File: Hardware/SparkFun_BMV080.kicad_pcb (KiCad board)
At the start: 2 copper layers, 25.4 x 14 mm, 37 parts, among them J1 Qwiic_RA, J2 Qwiic_RA, J3 Conn_01x06, J4 Conn_01x01, U1 BMV080

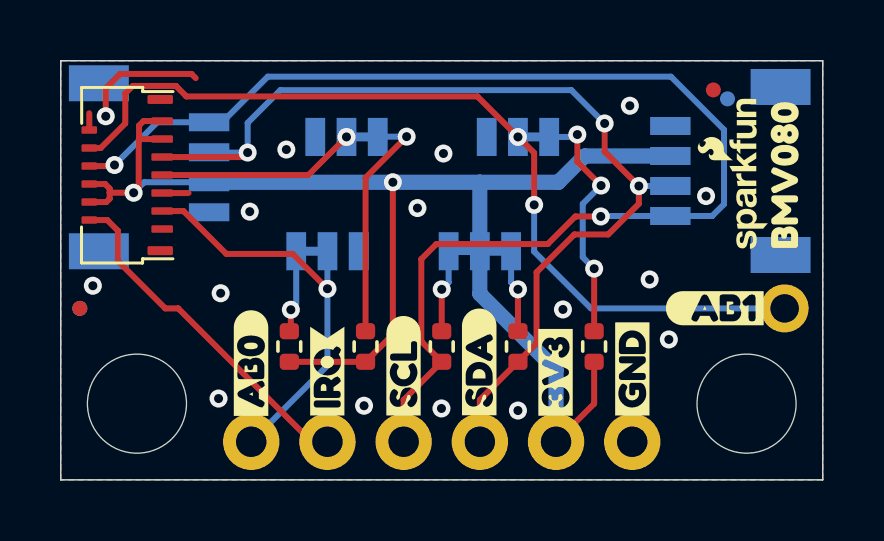
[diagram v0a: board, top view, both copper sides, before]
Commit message: schematic cleanup and reroute
-added section divider lines and section titles
-jumper reference and naming corrected, rotated text in sch to all horizontal
-added company and defined by:
-rearranged part name and value texts for calrity
-moved logos in sch to proper location
-moved to vertical qwiic connector
-added decoupling caps
-added exposed copper for potential heat sink
-added silk to jumpers
-added qwiic logo to silk
-added version v01 to bottom copper
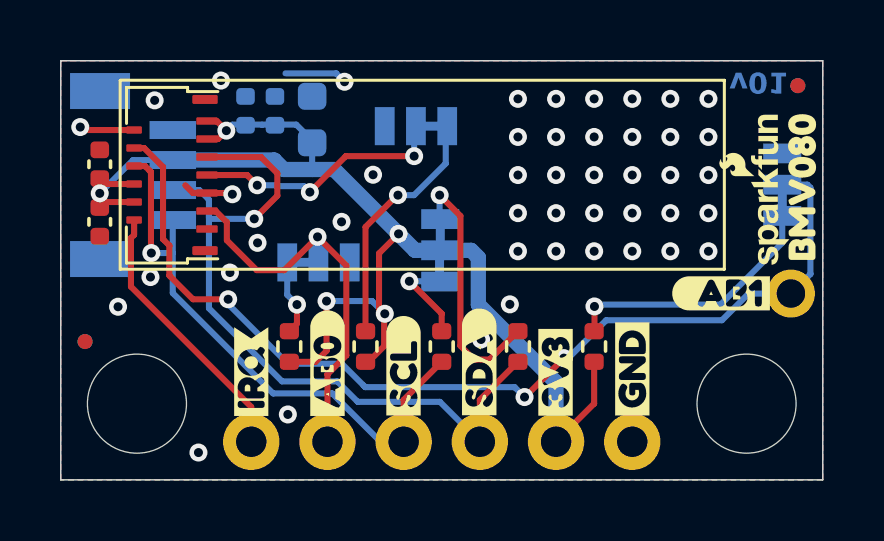
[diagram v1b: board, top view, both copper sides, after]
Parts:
- removed J1: Qwiic_RA, SparkFun-Connector:JST_SMD_1.0mm-4_RA
- added C1: 1.0uF, SparkFun-Capacitor:C_0402_1005Metric, F.Cu at (118.1, 93.6)
- added C2: 1.0uF, SparkFun-Capacitor:C_0402_1005Metric, F.Cu at (118.1, 95.5)
- added C3: 1.0uF, SparkFun-Capacitor:C_0402_1005Metric, B.Cu at (124.0, 91.8)
- added C4: 1.0uF, SparkFun-Capacitor:C_0402_1005Metric, B.Cu at (123.0, 91.8)
- added C5: 10uF, SparkFun-Capacitor:C_0603_1608Metric, B.Cu at (125.2, 92.1)
- added G***: LOGO, SparkFun-Aesthetic:qwiic_4mm, B.Cu at (119.2, 98.2)
- added kibuzzard-66C3B2A1: G***, kibuzzard-66C3B2A1, B.Cu at (128.7, 90.9)
- added kibuzzard-66C3B2DA: G***, kibuzzard-66C3B2DA, B.Cu at (125.5, 95.4)
- added kibuzzard-66C3B2FA: G***, kibuzzard-66C3B2FA, B.Cu at (140.9, 92.1)
- added kibuzzard-66C3B2FA: G***, kibuzzard-66C3B2FA, B.Cu at (127.6, 96.9)
- added kibuzzard-66C3B30A: G***, kibuzzard-66C3B30A, B.Cu at (123.4, 96.9)
- added kibuzzard-66C3B30A: G***, kibuzzard-66C3B30A, B.Cu at (140.9, 96.4)
- added kibuzzard-66C3B31E: G***, kibuzzard-66C3B31E, B.Cu at (139.4, 94.3)
- added kibuzzard-66C3B369: G***, kibuzzard-66C3B369, B.Cu at (131.0, 96.6)
- added kibuzzard-66C3B3B1: G***, kibuzzard-66C3B3B1, B.Cu at (126.4, 92.4)
- added kibuzzard-66C3B3D3: G***, kibuzzard-66C3B3D3, B.Cu at (131.0, 92.3)
- J2: value Qwiic_RA -> Qwiic_Vertical; footprint SparkFun-Connector:JST_SMD_1.0mm-4_RA -> SparkFun-Connector:JST_SMD_1.0mm-4_Vertical
- JP1: renamed from MODE1; value ~ -> MODE
- JP2: renamed from AB0; value ~ -> AB0
- JP3: renamed from AB1; value ~ -> AB1
- JP4: renamed from I2C1; value ~ -> I2C
- moved J2 18.1 mm to (119.1, 94.0)
- moved JP3 8.95 mm to (140.9, 94.3), turned to 90 degrees
- moved FID4 2.82 mm to (141.4, 91.0)
- moved kibuzzard-66BFC288 2.55 mm to (125.7, 100.2)
- moved kibuzzard-66BFC108 2.55 mm to (125.7, 100.2)
- moved kibuzzard-66BFC045 2.54 mm to (123.2, 100.5)
- moved kibuzzard-66BFC09F 2.54 mm to (123.2, 100.5)
- moved FID3 2.39 mm to (141.4, 91.0)
- moved JP1 2.34 mm to (128.7, 92.3)
- moved U1 1.50 mm to (120.5, 94.0)
- moved JP4 1.32 mm to (129.5, 96.5), turned to -90 degrees
- moved FID1 1.12 mm to (117.7, 99.5)
- moved FID2 1.12 mm to (117.7, 99.5)
- moved G*** 0.89 mm to (140.4, 94.5)
- moved kibuzzard-66BFB450 0.70 mm to (141.6, 94.4)
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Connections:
- J3 pad 1: AB0 -> IRQ
- J3 pad 2: IRQ -> AB0
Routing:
- net SCL: track 43.4 -> 19.4 mm, vias 2 -> 1
- net SDA: track 33.0 -> 25.1 mm, vias 3 -> 1
- net Net-(JP4-A): track 2.76 -> 8.61 mm
- net AB1: track 29.6 -> 33.6 mm, vias 2 -> 3
- net IRQ: track 11.6 -> 9.09 mm
- net 3.3V: track 46.7 -> 44.5 mm, vias 2 -> 5
- net Net-(JP1-C): track 6.67 -> 8.64 mm, vias 1 -> 3
- net Net-(JP3-A): track 8.26 -> 8.87 mm, vias 3 -> 1
- net GND: track 5.63 -> 5.62 mm, vias 16 -> 45
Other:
- board text added: "v01"

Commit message: changed bypass caps to larger value of 2.2uF
-bypass caps bumped up from 1.0uF to 2.2uF as per recommended in datasheet
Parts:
- C1, C2, C3, C4: value 1.0uF -> 2.2uF
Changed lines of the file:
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@@
 			)
 		)
-		(property "Value" "1.0uF"
+		(property "Value" "2.2uF"
 			(at 0 1.16 90)
 			(layer "F.Fab")
@@
 			)
 		)
-		(property "PROD_ID" "CAP-14969"
+		(property "PROD_ID" "CAP-14232"
 			(at 0 0 90)
 			(unlocked yes)
@@
 			)
 		)
-		(property "Voltage" "16V"
+		(property "Voltage" "10V"
 			(at 0 0 90)
 			(unlocked yes)
@@
 			)
 		)
-		(property "Value" "1.0uF"
+		(property "Value" "2.2uF"
 			(at 0 1.16 90)
 			(layer "F.Fab")
@@
 			)
 		)
-		(property "PROD_ID" "CAP-14969"
+		(property "PROD_ID" "CAP-14232"
 			(at 0 0 -90)
 			(unlocked yes)
@@
 			)
 		)
-		(property "Voltage" "16V"
+		(property "Voltage" "10V"
 			(at 0 0 -90)
 			(unlocked yes)
@@
 			)
 		)
-		(property "Value" "1.0uF"
+		(property "Value" "2.2uF"
 			(at 0 -1.16 90)
 			(layer "B.Fab")
@@
 			)
 		)
-		(property "PROD_ID" "CAP-14969"
+		(property "PROD_ID" "CAP-14232"
 			(at 0 0 -90)
 			(unlocked yes)
@@
 			)
 		)
-		(property "Voltage" "16V"
+		(property "Voltage" "10V"
 			(at 0 0 -90)
 			(unlocked yes)
@@
 			)
 		)
-		(property "Value" "1.0uF"
+		(property "Value" "2.2uF"
 			(at 0 -1.16 90)
 			(layer "B.Fab")
@@
 			)
 		)
-		(property "PROD_ID" "CAP-14969"
+		(property "PROD_ID" "CAP-14232"
 			(at 0 0 -90)
 			(unlocked yes)
@@
 			)
 		)
-		(property "Voltage" "16V"
+		(property "Voltage" "10V"
 			(at 0 0 -90)
 			(unlocked yes)

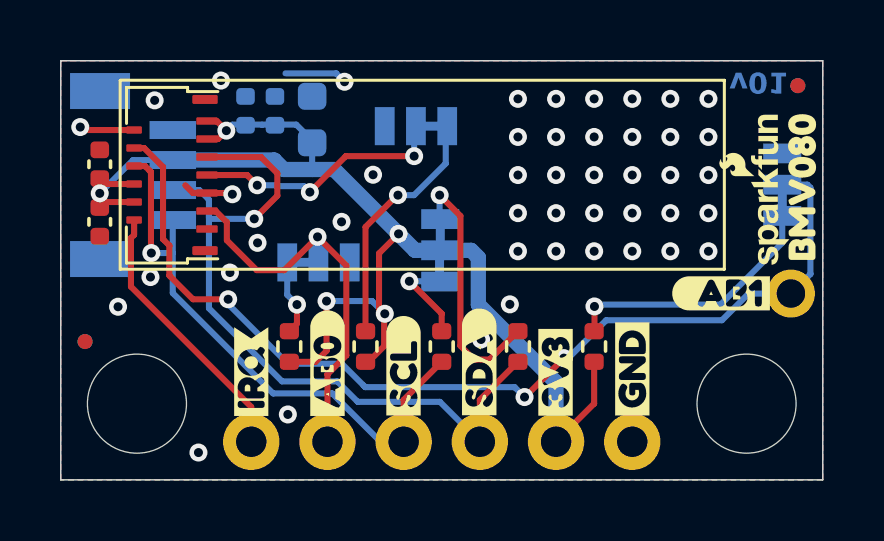
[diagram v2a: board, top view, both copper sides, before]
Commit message: jumpers to no silk outline and prod_id on ic
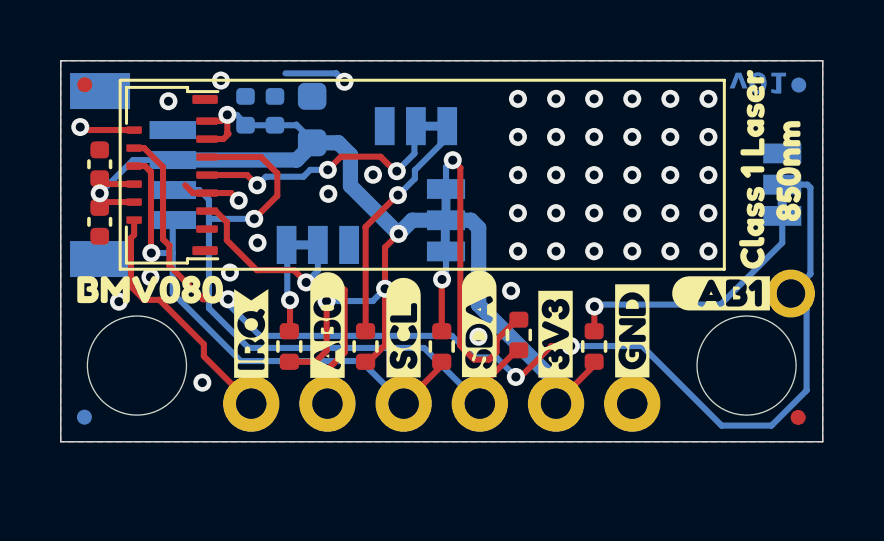
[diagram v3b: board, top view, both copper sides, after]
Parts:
- removed the G*** at (140.4, 94.5)
- added kibuzzard-66C4B812: G***, kibuzzard-66C4B812, F.Cu at (139.9, 93.8)
- added kibuzzard-66C4B81D: G***, kibuzzard-66C4B81D, F.Cu at (141.1, 93.8)
- JP1, JP2, JP3: footprint SparkFun-Jumper:Jumper_3_NC-1_Trace -> SparkFun-Jumper:Jumper_3_NC-1_Trace_NoSilk
- JP4: footprint SparkFun-Jumper:Jumper_3_NC-2_Trace -> SparkFun-Jumper:Jumper_3_NC-2_Trace_NoSilk
- moved FID2 23.9 mm to (141.4, 102.1)
- moved FID4 23.8 mm to (117.6, 91.0)
- moved kibuzzard-66BFB450 22.0 mm to (119.8, 97.8), turned to 0 degrees
- moved G*** 5.10 mm to (122.1, 94.0), turned to 90 degrees
- moved FID1 2.52 mm to (117.6, 102.0)
- moved J3 1.27 mm to (123.2, 101.6)
- moved kibuzzard-66BFBF23 1.27 mm to (130.8, 98.9)
- moved ST1 1.27 mm to (119.4, 100.3)
- moved ST2 1.27 mm to (139.7, 100.3)
- moved kibuzzard-66BFBF4E 1.27 mm to (128.3, 99.1)
- moved kibuzzard-66BFBF70 1.27 mm to (135.9, 99.2) (x2)
- moved kibuzzard-66BFBF9D 1.27 mm to (133.3, 99.3) (x2)
- moved kibuzzard-66BFC045 1.27 mm to (123.2, 99.3)
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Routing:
- net AB1: track 33.6 -> 37.7 mm
- net AB0: track 13.7 -> 11.5 mm
- net SCL: track 19.4 -> 17.6 mm
- net Net-(JP4-A): track 8.61 -> 10.3 mm
- net SDA: track 25.1 -> 23.8 mm
- net 3.3V: track 44.5 -> 43.4 mm
- net IRQ: track 9.09 -> 8.12 mm
- net GND: track 5.62 -> 5.92 mm, vias 45 -> 44
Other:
- board size 25.4 x 14 mm -> 25.4 x 12.7 mm

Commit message: measures and more
-add measures
-add copper finish
-add ordering instructions
-DRC fixes
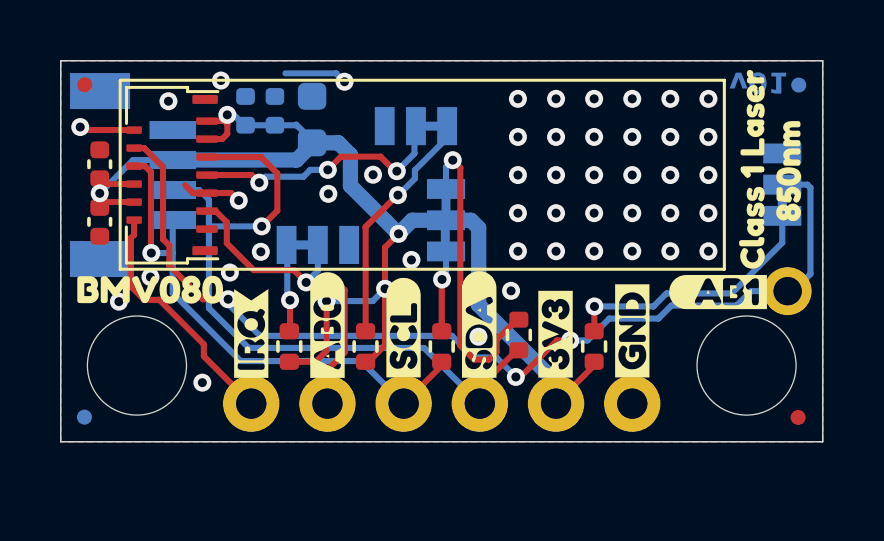
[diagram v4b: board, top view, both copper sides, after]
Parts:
- added G***: Flame, SparkFun-Aesthetic:SparkFun_Flame, F.Cu at (143.8, 95.4)
- moved J4 0.14 mm to (141.1, 97.8)
- moved kibuzzard-66BFC29E 0.11 mm to (138.8, 97.9)
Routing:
- net AB1: track 37.7 -> 32.8 mm
- net SDA: track 23.8 -> 24.4 mm
- net GND: vias 44 -> 45
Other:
- board text added: "Copper Weight: 1oz"
- board text added: "Finish: HAL Lead-free"
- board text added: "Layers: 2"
- board text added: "Material: TG155"
- board text added: "Ordering Notes"
- board text added: "Silkscreen Color: White"
- board text added: "Solder Mask: Black"
- board text added: "Thickness: 0.8mm"

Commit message: grid and molex connector FP correction
-set grid origin point to top left of PCB edge
-corrected molex connecto FP - width of mounting pads X position was 2.52 and now is 2.51
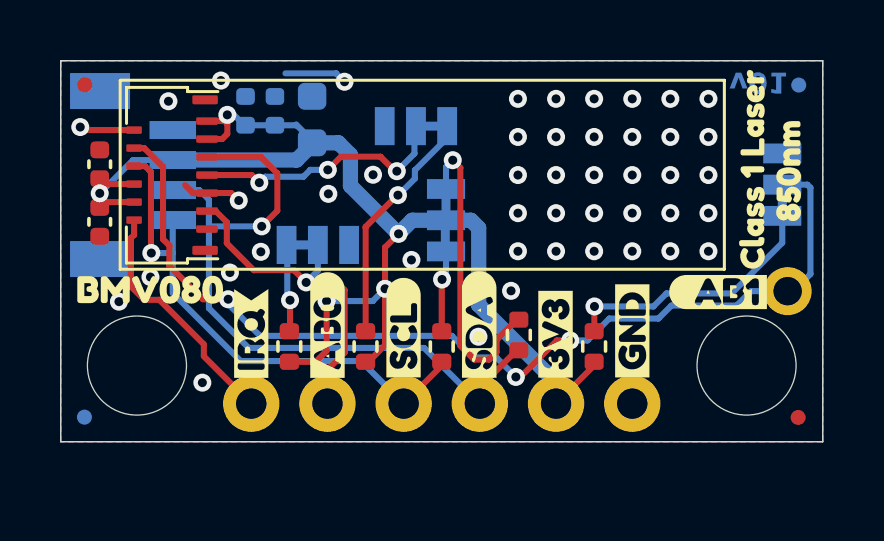
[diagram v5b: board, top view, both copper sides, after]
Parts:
- removed the G*** at (143.8, 95.4)
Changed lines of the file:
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@@
 		(pad_to_mask_clearance 0)
 		(allow_soldermask_bridges_in_footprints no)
+		(aux_axis_origin 116.84 90.17)
+		(grid_origin 116.84 90.17)
 		(pcbplotparams
 			(layerselection 0x00010fc_ffffffff)
@@
 		)
 	)
-	(footprint "SparkFun-Aesthetic:SparkFun_Flame"
-		(layer "F.Cu")
-		(at 143.85 95.38)
-		(tags "SparkFun")
-		(property "Reference" "G***"
-			(at 0 -2.54 0)
-			(layer "F.Fab")
-			(hide yes)
-			(effects
-				(font
-					(size 0.5 0.5)
-					(thickness 0.1)
-				)
-			)
-		)
-		(property "Value" "Flame"
-			(at 0 1.163333 0)
-			(layer "F.Fab")
-			(hide yes)
-			(effects
-				(font
-					(size 0.5 0.5)
-					(thickness 0.1)
-				)
-			)
-		)
-		(property "Footprint" "SparkFun-Aesthetic:SparkFun_Flame"
-			(at 0 0 0)
-			(unlocked yes)
-			(layer "F.Fab")
-			(hide yes)
-			(effects
-				(font
-					(size 1.27 1.27)
-					(thickness 0.15)
-				)
-			)
-		)
-		(property "Datasheet" ""
-			(at 0 0 0)
-			(unlocked yes)
-			(layer "F.Fab")
-			(hide yes)
-			(effects
-				(font
-					(size 1.27 1.27)
-					(thickness 0.15)
-				)
-			)
-		)
-		(property "Description" ""
-			(at 0 0 0)
-			(unlocked yes)
-			(layer "F.Fab")
-			(hide yes)
-			(effects
-				(font
-					(size 1.27 1.27)
-					(thickness 0.15)
-				)
-			)
-		)
-		(attr board_only exclude_from_pos_files exclude_from_bom)
-	)
 	(footprint "SparkFun-Resistor:R_0402_1005Metric"
 		(layer "F.Cu")
@@
 		)
 		(pad "M1" smd roundrect
-			(at -2.52 1.2 90)
+			(at -2.51 1.2 90)
 			(size 0.3 0.85)
 			(layers "F.Cu" "F.Paste" "F.Mask")
@@
 		)
 		(pad "M1" smd roundrect
-			(at 2.52 1.2 90)
+			(at 2.51 1.2 90)
 			(size 0.3 0.85)
 			(layers "F.Cu" "F.Paste" "F.Mask")
